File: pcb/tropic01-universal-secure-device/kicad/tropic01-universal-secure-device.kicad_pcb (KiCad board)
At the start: 6 copper layers, 42.7 x 36 mm, 90 parts, among them J1 USB4105-GF-A, J2 ER-TFT024IPS-3 50P FFC, J6 SM04B-SRSS-TB, J9 S2B-PH-SM4-TB, SW1 EVQP7J01P, U1 STM32U585VIT6, U10 BQ24074RGTR, U11 OPTIGA-TRUST-M-SLS32AIA, U13 TPS22917DBVR, U14 TPS22917DBVR, U15 TPS61165DBVR, U2 TR01-C2P-T301, U3 TPS62840DLCR, U4 TPS22917DBVR, U5 W25Q128JVSIQ, U7 TPD4E05U06DQAR, U8 TPS2553DBVR, U9 ST25R3916B-AQET, X1 16MHz, X3 FA-238 27.12MHz

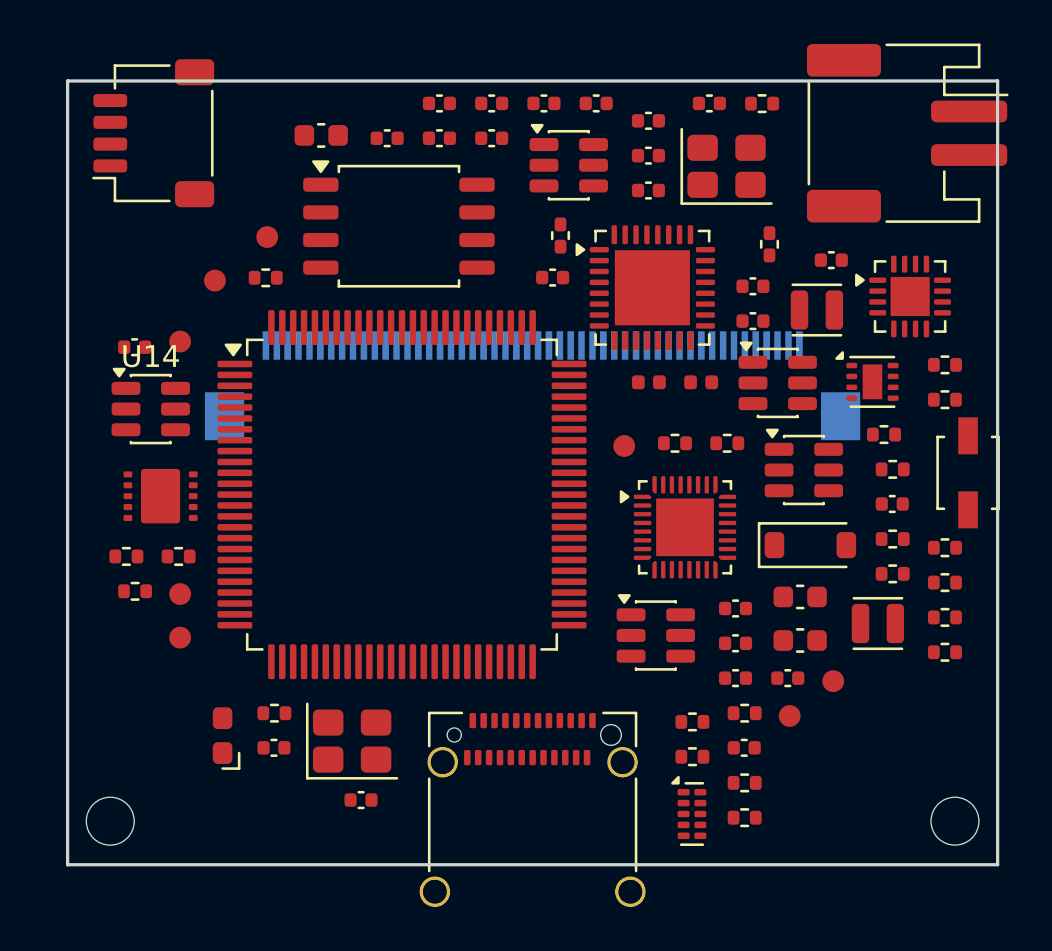
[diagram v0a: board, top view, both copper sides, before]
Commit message: fix(pcb): correct top connectors J6/J9 orientation + position
The two top connectors were rotated 90deg wrong (pin rows vertical = sideways)
and overhanging the top edge. Fixed:
- J6/J9 set to rot=180: pin rows horizontal (parallel to the top edge), cable
  mouth facing UP/out (same pattern as the bottom USB-C), fully on-board.
- NFC IC U9 moved off U1 (resolved pad shorts), STM32 raised off the USB-C.
- 0 courtyard/clearance overlaps; all perimeter constraints held.
Battery connector kept as JST-PH 2.0mm (J9) - the de-facto LiPo standard.
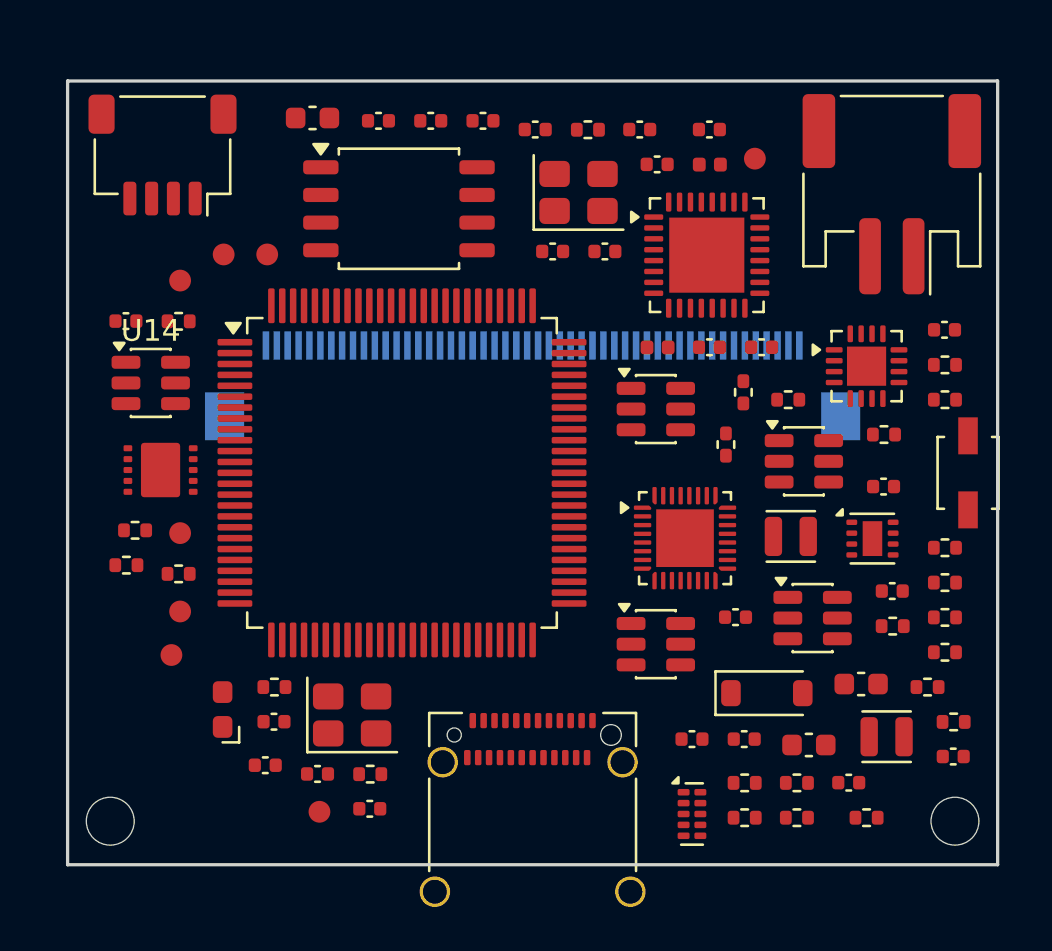
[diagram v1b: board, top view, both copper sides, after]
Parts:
- moved C8 38.2 mm to (51.3, 65.0)
- moved C16 29.3 mm to (19.7, 65.4)
- moved TP_3V3 25.6 mm to (42.2, 37.6)
- moved R16 24.7 mm to (48.5, 59.0)
- moved TP_GND 24.4 mm to (22.2, 67.6)
- moved C41 24.3 mm to (48.5, 57.4)
- moved U13 23.6 mm to (44.9, 58.7)
- moved TP_BOOT0 20.8 mm to (15.8, 54.8)
- moved TP_SWDIO 19.7 mm to (15.4, 60.4)
- moved R15 19.5 mm to (34.5, 36.2)
- moved TP_UART_TX 18.0 mm to (19.8, 42.0)
- moved C17 17.4 mm to (24.5, 67.4)
- moved R5 17.4 mm to (24.5, 65.8)
- moved R22 13.1 mm to (13.7, 54.6)
- moved R7 12.6 mm to (15.7, 45.0)
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
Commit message: feat(pcb): switch stackup 6-layer -> 4-layer (cost + standard)
Evidence-based decision: a routing comparison showed 4 layers
(F/GND-plane/In2/B = 3 signal + 1 GND plane) routes this board as well as
6 layers (same ~17 unrouted raw) - the routing bottleneck is fine-pitch IC
pin-escape congestion, NOT layer count or placement. So drop to 4 layers:
cheaper at PCBWay and the more common/standard stackup, with no routing loss.

Also verified (separately): a pin-aware re-placement (STM32 rot270 for a short
USB pair, peripherals at the MCU's pin clusters) yields the SAME routing result,
confirming the current clean placement is already good enough; kept it for
simplicity + reliability. The ~17 remaining nets are pin-escape-limited and need
the routing-finish pass regardless of stackup/placement.
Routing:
- removed copper zone on In4.Cu, net GND
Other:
- copper layers 6 -> 4
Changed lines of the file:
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@@
 	(layers
 		(0 "F.Cu" signal)
-		(4 "In1.Cu" power "GND1")
+		(4 "In1.Cu" power "GND")
 		(6 "In2.Cu" signal)
-		(8 "In3.Cu" signal)
-		(10 "In4.Cu" power "GND2")
 		(2 "B.Cu" signal)
 		(9 "F.Adhes" user "F.Adhesive")
@@
 		(polygon
 			(pts
-				(xy 10.94 34.3) (xy 53.06 34.3) (xy 53.06 69.7) (xy 10.94 69.7)
-			)
-		)
-	)
-	(zone
-		(net "GND")
-		(layer "In4.Cu")
-		(hatch edge 0.5)
-		(connect_pads
-			(clearance 0.2)
-		)
-		(min_thickness 0.18)
-		(fill yes
-			(thermal_gap 0.5)
-			(thermal_bridge_width 0.5)
-			(island_removal_mode 0)
-		)
-		(polygon
-			(pts
-				(xy 10.94 34.3) (xy 53.06 34.3) (xy 53.06 69.7) (xy 10.94 69.7)
+				(xy 10.865 34.225) (xy 53.135 34.225) (xy 53.135 69.775) (xy 10.865 69.775)
 			)
 		)

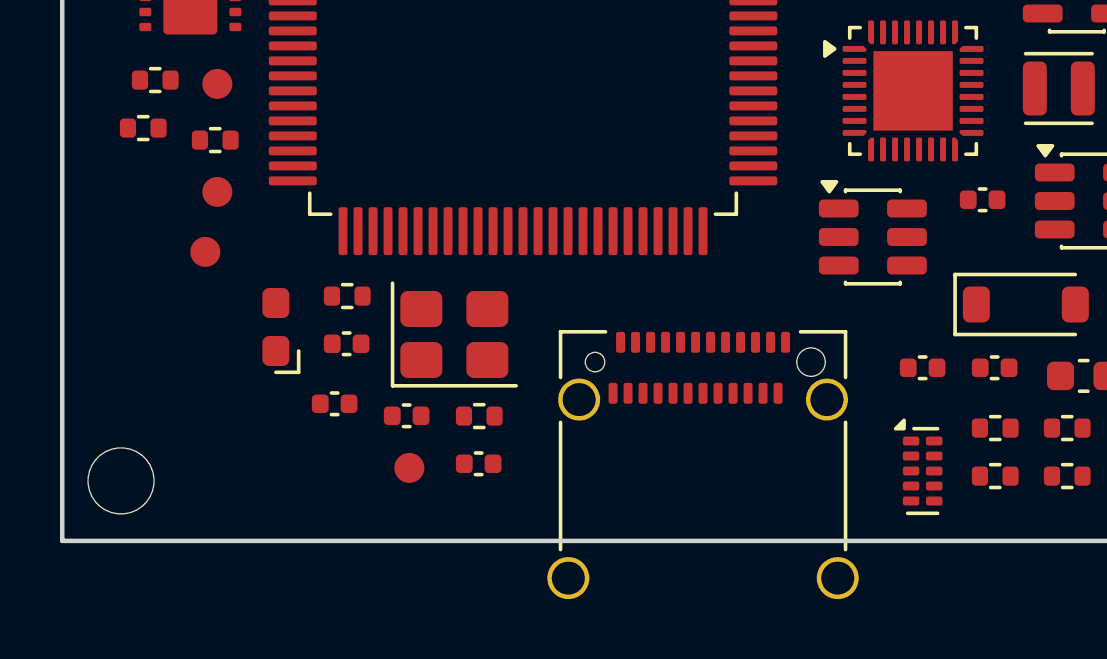
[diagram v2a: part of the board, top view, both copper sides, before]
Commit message: fix(pcb): move USB-C up so its shield posts sit on the board
J1 (USB4105-GF-A) was placed too low: the connector overhung the bottom edge
by ~4mm and 2 of its 4 through-hole shield/mounting posts (Y71.2) fell ~1mm
OUTSIDE the board outline (Y70.1) - no copper to solder to (would fail fab and
leave the connector mechanically weak). Move J1 up 1.5mm (Y68.4->66.9): all
solder features (24 SMD pads + 2 NPTH locating pegs + 4 PTH shield posts) are
now on-board, while the cable-mating lip still overhangs the edge (correct, so
the plug inserts from outside). Relocated U4 (the one part it now overlapped).
0 courtyard/clearance overlaps.
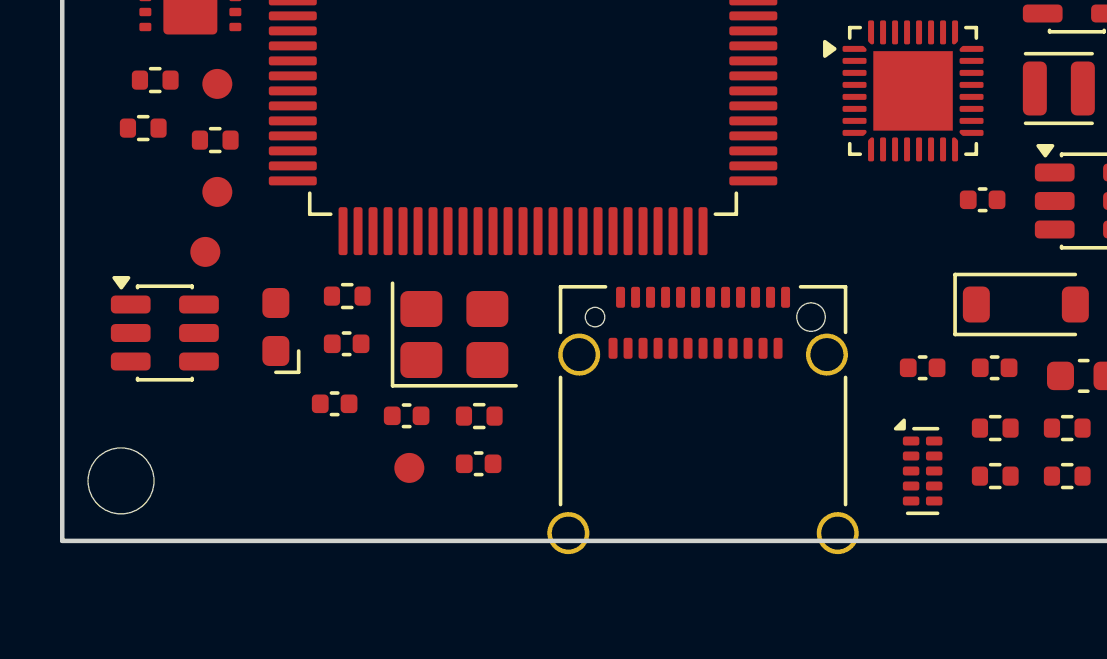
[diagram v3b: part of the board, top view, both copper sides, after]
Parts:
- moved U4 23.8 mm to (14.1, 63.1)
- moved J1 1.50 mm to (32.0, 66.9)
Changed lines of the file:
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@@
 	(footprint "Connector_USB:USB_C_Receptacle_GCT_USB4105-xx-A_16P_TopMnt_Horizontal"
 		(layer "F.Cu")
-		(at 32 68.4)
+		(at 32 66.9)
 		(descr "GCT USB4105 USB 2.0 Type-C receptacle; female USB-C only, centered on bottom short edge")
 		(tags "USB C Type-C Receptacle SMD")
@@
 	(footprint "Package_TO_SOT_SMD:SOT-23-6"
 		(layer "F.Cu")
-		(at 37.659999 59.869999)
+		(at 14.059999 63.069999)
 		(descr "SOT, 6 Pin (JEDEC MO-178 Var AB https://www.jedec.org/document_search?search_api_views_fulltext=MO-178)")
 		(tags "SOT TO_SOT_SMD")

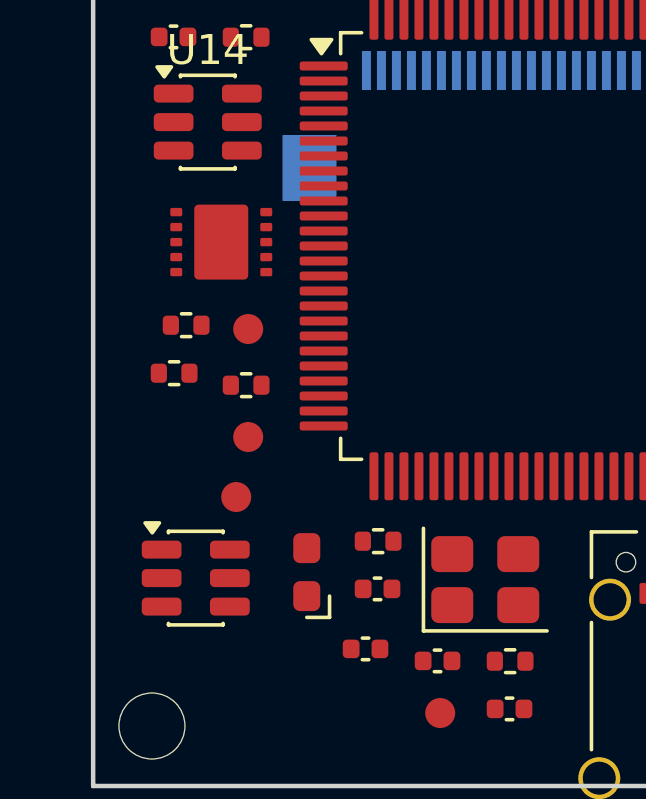
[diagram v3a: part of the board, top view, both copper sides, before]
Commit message: fix(pcb): make status LED top-emitting and move it opposite the button
LED1 was APA1606SURCK on the *right-angled* footprint
(LED_Kingbright_APA1606_1.6x0.6mm_Horizontal) - a SIDE-emitting part, so its
light shot out the board edge instead of up. Swap to a top-view 0603 LED
(LED_0603_1608Metric, KP-1608SURCK) so it emits perpendicular to the board
(straight up out of the surface). Relocate from the bottom-left/USB-C area to
(12.0, 52.0) - center-left edge, mirror of the SW1 button (center-right). Nets
preserved (anode=LED_STATUS_LED, cathode=GND); no courtyard overlap; 0.6mm off
the left edge.
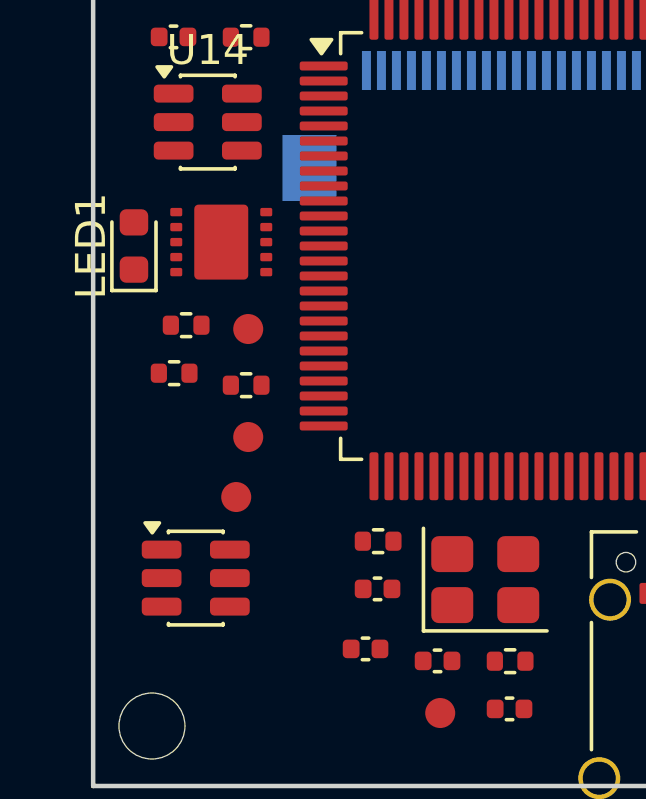
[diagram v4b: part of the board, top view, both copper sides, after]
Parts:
- LED1: value APA1606SURCK -> KP-1608SURCK; footprint LED_SMD:LED_Kingbright_APA1606_1.6x0.6mm_Horizontal -> LED_0603_1608Metric
- moved LED1 12.3 mm to (12.0, 52.0)
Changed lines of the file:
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@@
 		)
 	)
-	(footprint "LED_SMD:LED_Kingbright_APA1606_1.6x0.6mm_Horizontal"
-		(layer "F.Cu")
-		(at 17.759999 62.869999 90)
-		(descr "Right angled LED, 1.6x1.2 mm, H0.6 mm")
-		(tags "LED chip right angled vertical")
-		(property "Reference" "LED1"
-			(at 0 -1.9 0)
-			(layer "F.SilkS")
-			(hide yes)
-			(effects
-				(font
-					(size 1 1)
-					(thickness 0.15)
-				)
-			)
-		)
-		(property "Value" "APA1606SURCK"
-			(at 0 1.6 0)
-			(layer "F.Fab")
-			(effects
-				(font
-					(size 1 1)
-					(thickness 0.15)
-				)
-			)
-		)
-		(property "Datasheet" ""
-			(at 0 0 0)
-			(unlocked yes)
-			(layer "F.Fab")
-			(hide yes)
-			(effects
-				(font
-					(size 1.27 1.27)
-					(thickness 0.15)
-				)
-			)
-		)
-		(property "Description" ""
-			(at 0 0 0)
-			(unlocked yes)
-			(layer "F.Fab")
-			(hide yes)
-			(effects
-				(font
-					(size 1.27 1.27)
-					(thickness 0.15)
-				)
-			)
-		)
-		(attr smd)
-		(duplicate_pad_numbers_are_jumpers no)
-		(fp_line
-			(start -1.51 0)
-			(end -1.51 0.76)
-			(stroke
-				(width 0.12)
-				(type default)
-			)
-			(layer "F.SilkS")
-		)
-		(fp_line
-			(start -1.51 0.76)
-			(end -0.8 0.76)
-			(stroke
-				(width 0.12)
-				(type default)
-			)
-			(layer "F.SilkS")
-		)
-		(fp_poly
-			(pts
-				(xy -0.8 -1.15) (xy 0.8 -1.15) (xy 0.8 -0.75) (xy 1.5 -0.75) (xy 1.5 0.75) (xy -1.5 0.75) (xy -1.5 -0.75)
-				(xy -0.8 -0.75)
-			)
-			(stroke
-				(width 0.05)
-				(type solid)
-			)
-			(fill no)
-			(layer "F.CrtYd")
-		)
-		(fp_line
-			(start -0.55 -0.9)
-			(end 0.55 -0.9)
-			(stroke
-				(width 0.1)
-				(type default)
-			)
-			(layer "F.Fab")
-		)
-		(fp_line
-			(start 0.8 -0.3)
-			(end 0.8 0.3)
-			(stroke
-				(width 0.1)
-				(type default)
-			)
-			(layer "F.Fab")
-		)
-		(fp_line
-			(start 0.6 -0.3)
-			(end 0.55 -0.9)
-			(stroke
-				(width 0.1)
-				(type default)
-			)
-			(layer "F.Fab")
-		)
-		(fp_line
-			(start -0.6 -0.3)
-			(end -0.55 -0.9)
-			(stroke
-				(width 0.1)
-				(type default)
-			)
-			(layer "F.Fab")
-		)
-		(fp_line
-			(start -0.8 -0.3)
-			(end 0.8 -0.3)
-			(stroke
-				(width 0.1)
-				(type default)
-			)
-			(layer "F.Fab")
-		)
-		(fp_line
-			(start -0.8 0.1)
-			(end -0.8 -0.3)
-			(stroke
-				(width 0.1)
-				(type default)
-			)
-			(layer "F.Fab")
-		)
-		(fp_line
-			(start 0.8 0.3)
-			(end -0.6 0.3)
-			(stroke
-				(width 0.1)
-				(type default)
-			)
-			(layer "F.Fab")
-		)
-		(fp_line
-			(start -0.6 0.3)
-			(end -0.8 0.1)
-			(stroke
-				(width 0.1)
-				(type default)
-			)
-			(layer "F.Fab")
-		)
-		(fp_text user "${REFERENCE}"
-			(at 0 0 0)
-			(layer "F.Fab")
-			(effects
-				(font
-					(size 0.25 0.25)
-					(thickness 0.04)
-				)
-			)
-		)
-		(pad "1" smd roundrect
-			(at -0.8 0)
-			(size 0.9 1)
-			(layers "F.Cu" "F.Mask" "F.Paste")
-			(roundrect_rratio 0.25)
-			(net "LED_STATUS_LED")
-			(thermal_bridge_angle 45)
-		)
-		(pad "2" smd roundrect
-			(at 0.8 0)
-			(size 0.9 1)
-			(layers "F.Cu" "F.Mask" "F.Paste")
-			(roundrect_rratio 0.25)
-			(net "GND")
-			(thermal_bridge_angle 45)
-		)
-		(embedded_fonts no)
-		(model "${KICAD10_3DMODEL_DIR}/LED_SMD.3dshapes/LED_Kingbright_APA1606_1.6x0.6mm_Horizontal.step"
-			(offset
-				(xyz 0 0 0)
-			)
-			(scale
-				(xyz 1 1 1)
-			)
-			(rotate
-				(xyz 0 0 0)
-			)
-		)
-	)
 	(footprint "Capacitor_SMD:C_0402_1005Metric"
 		(layer "F.Cu")
@@
 			(offset
 				(xyz 0 0 0)
+			)
+			(scale
+				(xyz 1 1 1)
+			)
+			(rotate
+				(xyz 0 0 0)
+			)
+		)
+	)
+	(footprint "LED_0603_1608Metric"
+		(layer "F.Cu")
+		(at 12 52 90)
+		(descr "LED SMD 0603 (1608 Metric), square (rectangular) end terminal, IPC-7351 nominal, (Body size source: http://www.tortai-tech.com/upload/download/2011102023233369053.pdf)")
+		(tags "LED")
+		(property "Reference" "LED1"
+			(at 0 -1.43 90)
+			(layer "F.SilkS")
+			(effects
+				(font
+					(size 1 1)
+					(thickness 0.15)
+				)
+			)
+		)
+		(property "Value" "KP-1608SURCK"
+			(at 0 1.43 90)
+			(layer "F.Fab")
+			(effects
+				(font
+					(size 1 1)
+					(thickness 0.15)
+				)
+			)
+		)
+		(property "Datasheet" ""
+			(at 0 0 90)
+			(layer "F.Fab")
+			(hide yes)
+			(effects
+				(font
+					(size 1.27 1.27)
+				)
+			)
+		)
+		(property "Description" ""
+			(at 0 0 90)
+			(layer "F.Fab")
+			(hide yes)
+			(effects
+				(font
+					(size 1.27 1.27)
+				)
+			)
+		)
+		(property "KiLib_Generator" "SMD_2terminal_chip_molded"
+			(at 0 0 90)
+			(layer "F.SilkS")
+			(hide yes)
+			(effects
+				(font
+					(size 1 1)
+					(thickness 0.15)
+				)
+			)
+		)
+		(attr smd)
+		(duplicate_pad_numbers_are_jumpers no)
+		(fp_line
+			(start 0.8 -0.735)
+			(end -1.485 -0.735)
+			(stroke
+				(width 0.12)
+				(type solid)
+			)
+			(layer "F.SilkS")
+		)
+		(fp_line
+			(start -1.485 -0.735)
+			(end -1.485 0.735)
+			(stroke
+				(width 0.12)
+				(type solid)
+			)
+			(layer "F.SilkS")
+		)
+		(fp_line
+			(start -1.485 0.735)
+			(end 0.8 0.735)
+			(stroke
+				(width 0.12)
+				(type solid)
+			)
+			(layer "F.SilkS")
+		)
+		(fp_rect
+			(start -1.48 -0.73)
+			(end 1.48 0.73)
+			(stroke
+				(width 0.05)
+				(type solid)
+			)
+			(fill no)
+			(layer "F.CrtYd")
+		)
+		(fp_line
+			(start 0.8 -0.4)
+			(end -0.5 -0.4)
+			(stroke
+				(width 0.1)
+				(type solid)
+			)
+			(layer "F.Fab")
+		)
+		(fp_line
+			(start -0.5 -0.4)
+			(end -0.8 -0.1)
+			(stroke
+				(width 0.1)
+				(type solid)
+			)
+			(layer "F.Fab")
+		)
+		(fp_line
+			(start -0.8 -0.1)
+			(end -0.8 0.4)
+			(stroke
+				(width 0.1)
+				(type solid)
+			)
+			(layer "F.Fab")
+		)
+		(fp_line
+			(start 0.8 0.4)
+			(end 0.8 -0.4)
+			(stroke
+				(width 0.1)
+				(type solid)
+			)
+			(layer "F.Fab")
+		)
+		(fp_line
+			(start -0.8 0.4)
+			(end 0.8 0.4)
+			(stroke
+				(width 0.1)
+				(type solid)
+			)
+			(layer "F.Fab")
+		)
+		(fp_text user "${REFERENCE}"
+			(at 0 0 90)
+			(layer "F.Fab")
+			(effects
+				(font
+					(size 0.4 0.4)
+					(thickness 0.06)
+				)
+			)
+		)
+		(pad "1" smd roundrect
+			(at -0.7875 0 90)
+			(size 0.875 0.95)
+			(layers "F.Cu" "F.Mask" "F.Paste")
+			(roundrect_rratio 0.25)
+			(net "LED_STATUS_LED")
+		)
+		(pad "2" smd roundrect
+			(at 0.7875 0 90)
+			(size 0.875 0.95)
+			(layers "F.Cu" "F.Mask" "F.Paste")
+			(roundrect_rratio 0.25)
+			(net "GND")
+		)
+		(embedded_fonts no)
+		(model "${KICAD10_3DMODEL_DIR}/LED_SMD.3dshapes/LED_0603_1608Metric.step"
+			(offset
+				(xyz 0 0 0)
